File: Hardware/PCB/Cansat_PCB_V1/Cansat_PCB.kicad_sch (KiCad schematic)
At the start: 50 parts, among them J1 Lecteur SD, SW1 RSTBTN, SW2 boot, U1 Baro BMP581, U2 STM32G431CBUx, U3 IMU BNO055, U4 Adaptateur USB, Y1 Crystal_GND24_Small, Y2 Oscillateur_IMU

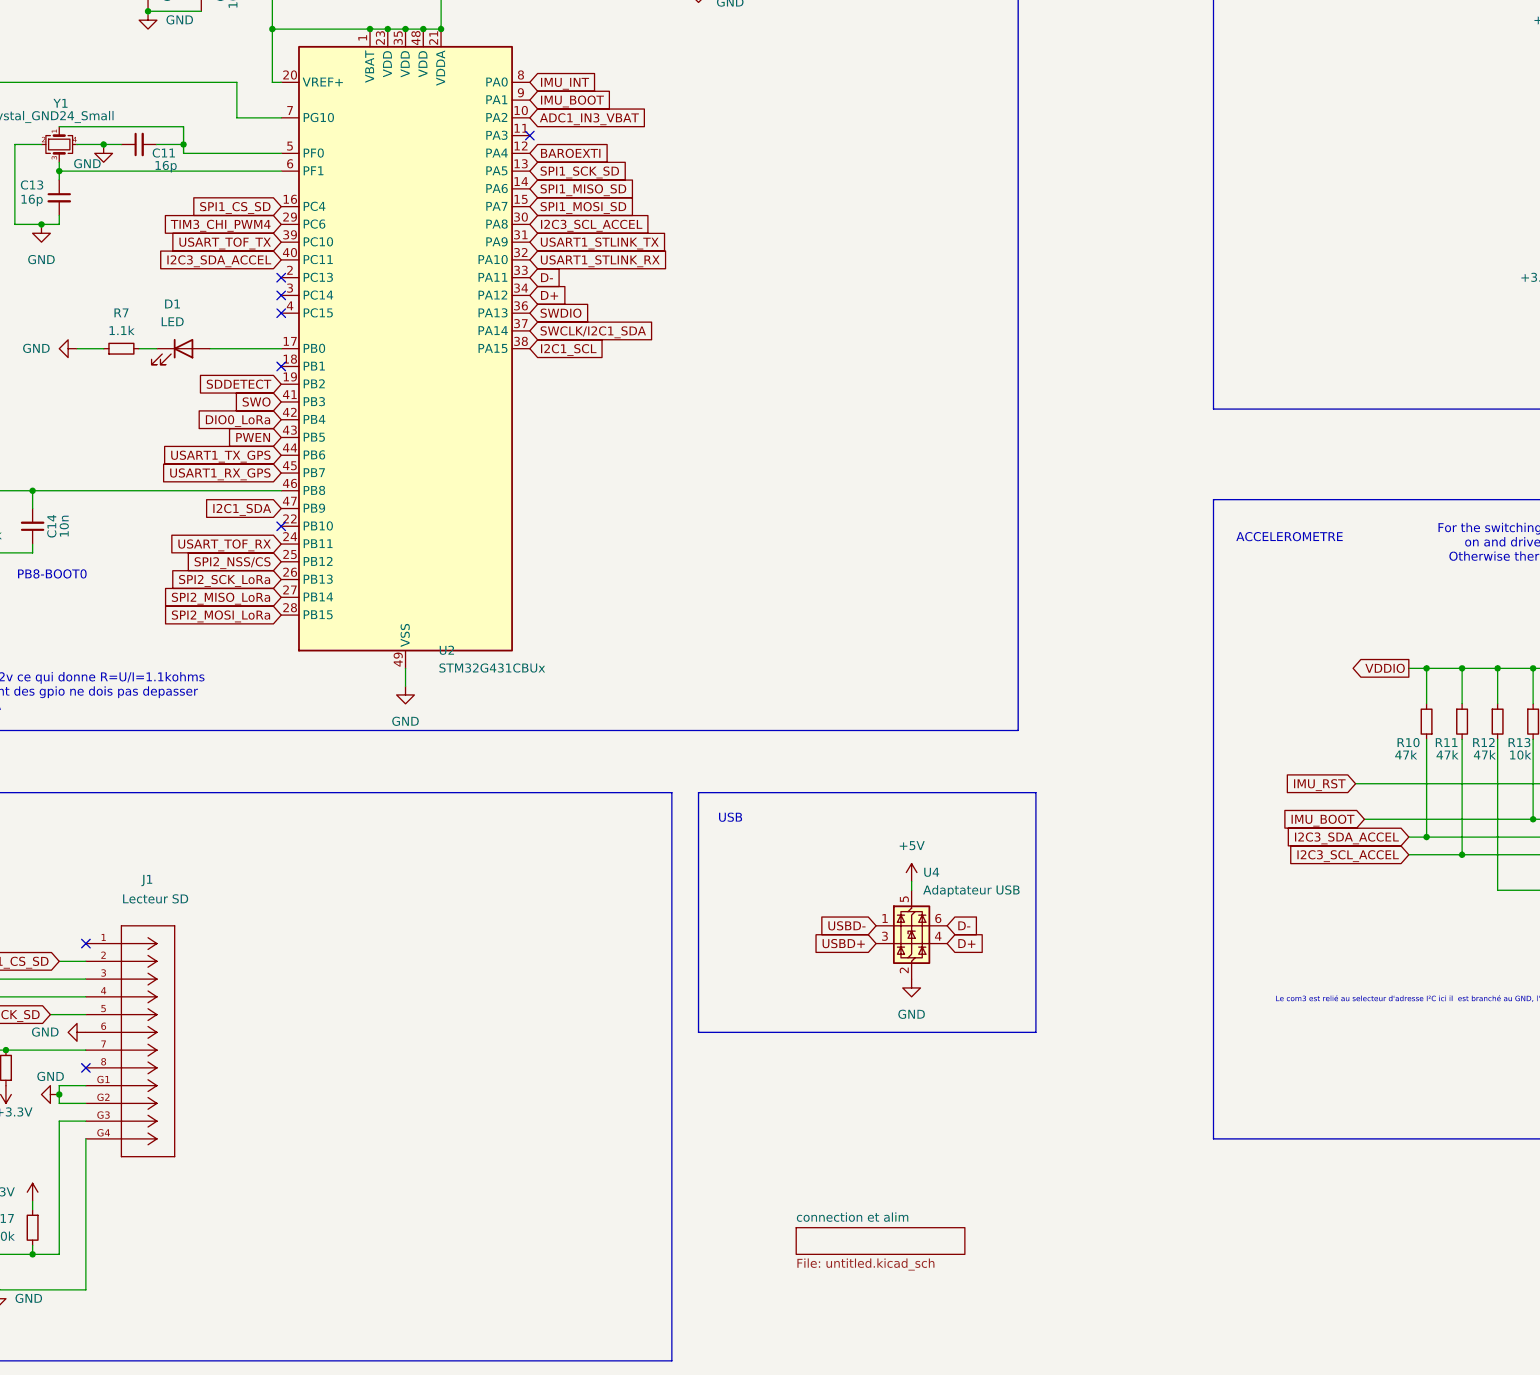
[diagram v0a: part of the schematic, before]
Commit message: ajout 2 Led adr + btn cmd + buck LMR51625 => sch complet sans warnings et erreurs
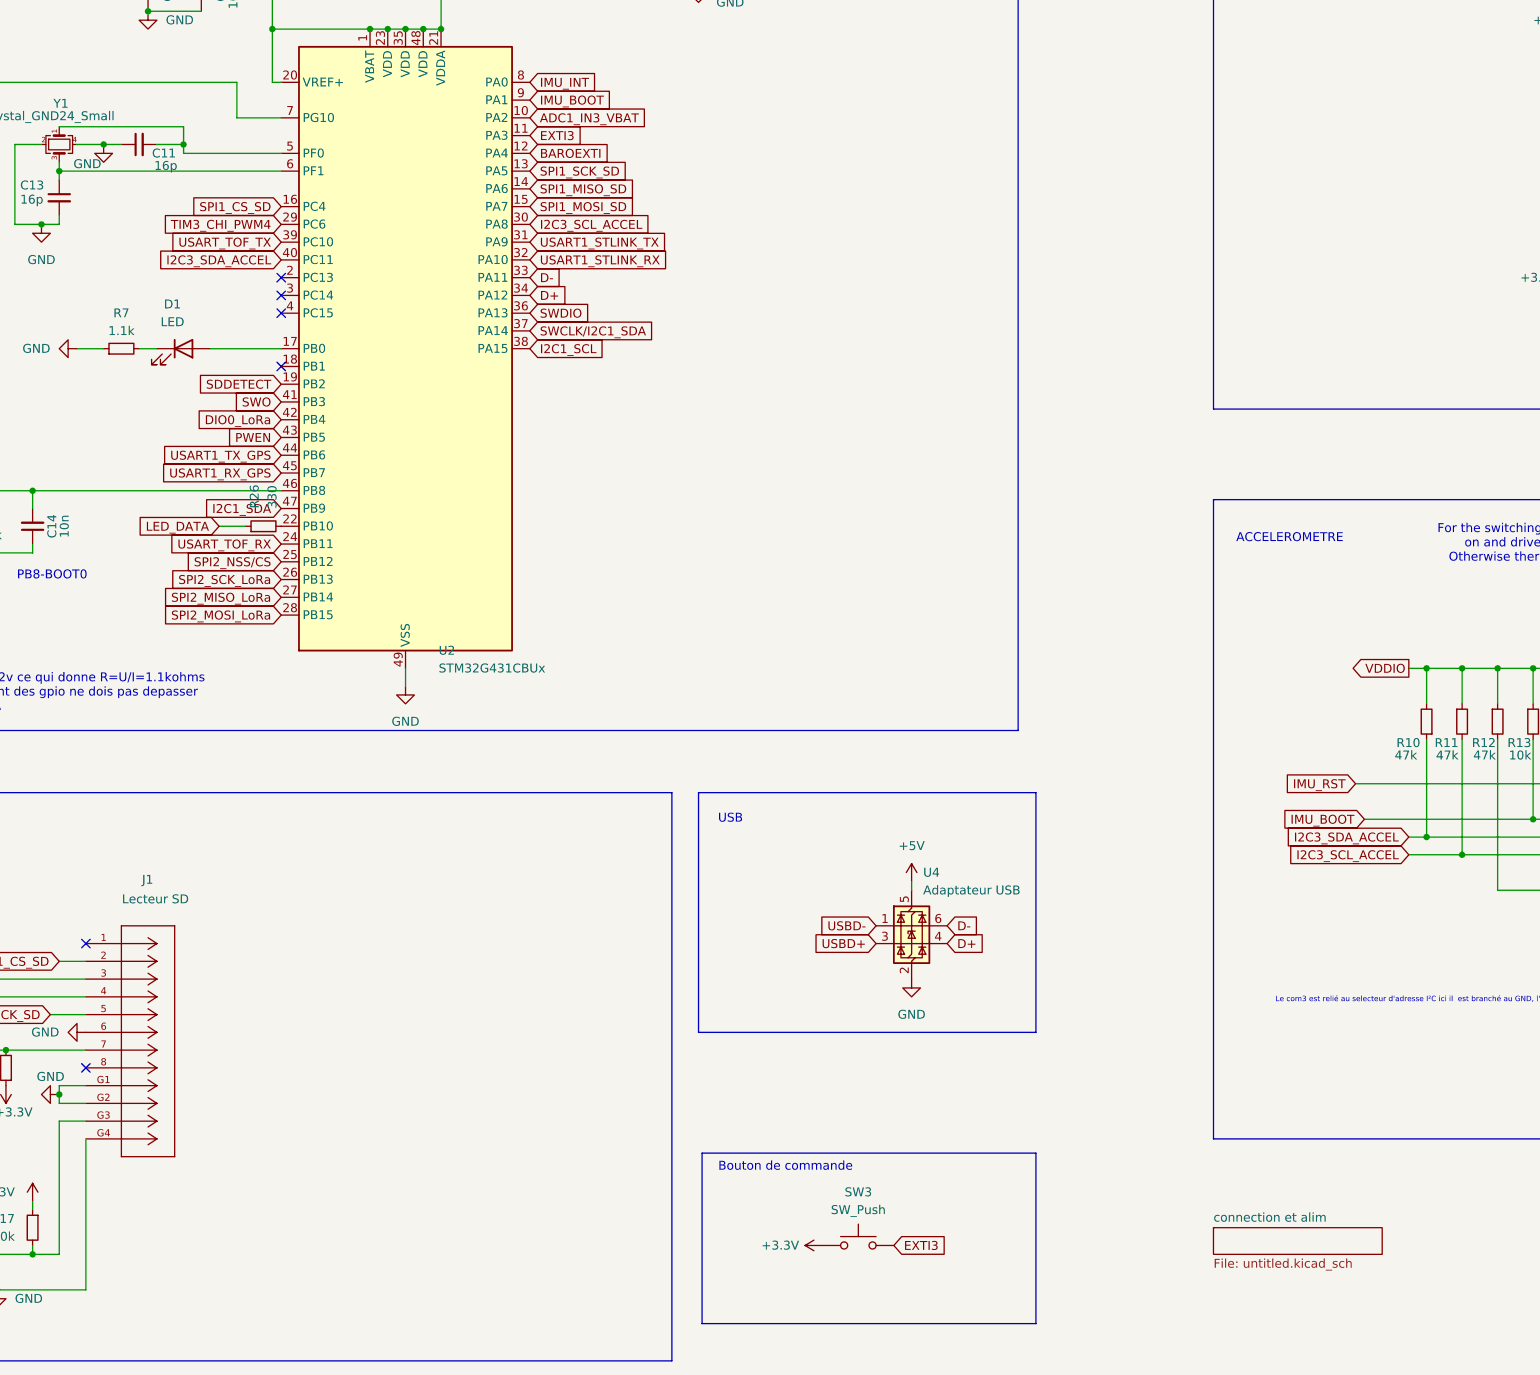
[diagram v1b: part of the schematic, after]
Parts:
- added R26: 330, Resistor_SMD:R_0402_1005Metric_Pad0.72x0.64mm_HandSolder, symbol Device:R_Small
- added SW3: SW_Push, Button_Switch_SMD:SW_Push_1P1T_NO_CK_PTS125Sx43PSMTR, symbol Switch:SW_Push
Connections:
- net +3.3V: now also SW3.1
- net EXTI3: now reaches U2.11 (PA3)
- net EXTI3: now also SW3.2
- net at U2.22 (PB10): now also R26.2
- new net LED_DATA: R26.1
- no-connect marks 12 -> 10
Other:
- note added: "Bouton de commande"

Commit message: routage non fini : ceci est un commit de transfert de fichier vers un autre PC
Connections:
- net VDDIO is gone; now on net +3.3V: C15.2, R10.2, R11.1, R12.1, R13.1, R14.1, U3.28 (VDDIO)
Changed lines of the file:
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@@
 	)
 	(junction
+		(at 340.36 149.86)
+		(diameter 0)
+		(color 0 0 0 0)
+	)
+	(junction
 		(at 320.04 87.63)
 		(diameter 0)
@@
 	)
 	(junction
-		(at 328.93 149.86)
-		(diameter 0)
-		(color 0 0 0 0)
-	)
-	(junction
 		(at 132.08 58.42)
 		(diameter 0)
@@
 	(wire
 		(pts
-			(xy 300.99 149.86) (xy 328.93 149.86)
-		)
-		(stroke
-			(width 0)
-			(type default)
-		)
-	)
-	(wire
-		(pts
 			(xy 77.47 204.47) (xy 88.9 204.47)
 		)
@@
 	(wire
 		(pts
+			(xy 340.36 149.86) (xy 356.87 149.86)
+		)
+		(stroke
+			(width 0)
+			(type default)
+		)
+	)
+	(wire
+		(pts
 			(xy 85.09 78.74) (xy 116.84 78.74)
 		)
@@
 	(wire
 		(pts
-			(xy 328.93 149.86) (xy 356.87 149.86)
+			(xy 300.99 149.86) (xy 340.36 149.86)
 		)
 		(stroke
@@
 	)
 	(symbol
+		(lib_id "power:+3.3V")
+		(at 340.36 149.86 0)
+		(unit 1)
+		(exclude_from_sim no)
+		(in_bom yes)
+		(on_board yes)
+		(dnp no)
+		(property "Reference" "#PWR041"
+			(at 340.36 153.67 0)
+			(effects
+				(font
+					(size 1.27 1.27)
+				)
+				(hide yes)
+			)
+		)
+		(property "Value" "+3.3V"
+			(at 336.55 146.05 0)
+			(effects
+				(font
+					(size 1.27 1.27)
+				)
+				(justify left)
+			)
+		)
+		(property "Footprint" ""
+			(at 340.36 149.86 0)
+			(effects
+				(font
+					(size 1.27 1.27)
+				)
+				(hide yes)
+			)
+		)
+		(property "Datasheet" ""
+			(at 340.36 149.86 0)
+			(effects
+				(font
+					(size 1.27 1.27)
+				)
+				(hide yes)
+			)
+		)
+		(property "Description" "Power symbol creates a global label with name \"+3.3V\""
+			(at 340.36 149.86 0)
+			(effects
+				(font
+					(size 1.27 1.27)
+				)
+				(hide yes)
+			)
+		)
+		(pin "1"
+		)
+		(instances
+			(project "Cansat_PCB"
+				(path "/43b9f51a-edfb-48c9-aab9-a28c7efe9297"
+					(reference "#PWR041")
+					(unit 1)
+				)
+			)
+		)
+	)
+	(symbol
 		(lib_id "Device:C_Small")
 		(at 96.52 74.93 90)
@@
 					(unit 1)
 				)
-			)
-		)
-	)
-	(symbol
-		(lib_id "power:PWR_FLAG")
-		(at 328.93 149.86 0)
-		(unit 1)
-		(exclude_from_sim no)
-		(in_bom yes)
-		(on_board yes)
-		(dnp no)
-		(fields_autoplaced yes)
-		(property "Reference" "#FLG03"
-			(at 328.93 147.955 0)
-			(effects
-				(font
-					(size 1.27 1.27)
-				)
-				(hide yes)
-			)
-		)
-		(property "Value" "PWR_FLAG"
-			(at 328.93 144.78 0)
-			(effects
-				(font
-					(size 1.27 1.27)
-				)
-			)
-		)
-		(property "Footprint" ""
-			(at 328.93 149.86 0)
-			(effects
-				(font
-					(size 1.27 1.27)
-				)
-				(hide yes)
-			)
-		)
-		(property "Datasheet" "~"
-			(at 328.93 149.86 0)
-			(effects
-				(font
-					(size 1.27 1.27)
-				)
-				(hide yes)
-			)
-		)
-		(property "Description" "Special symbol for telling ERC where power comes from"
-			(at 328.93 149.86 0)
-			(effects
-				(font
-					(size 1.27 1.27)
-				)
-				(hide yes)
-			)
-		)
-		(pin "1"
-		)
-		(instances
-			(project "Cansat_PCB"
-				(path "/43b9f51a-edfb-48c9-aab9-a28c7efe9297"
-					(reference "#FLG03")
-					(unit 1)
-				)

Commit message: nouvelles règles de routage Attention les pistes sont à l'ancienne taille : a corriger
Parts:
- removed SW3: SW_Push, Button_Switch_SMD:SW_Push_1P1T_NO_CK_PTS125Sx43PSMTR, symbol Switch:SW_Push
- removed U4: Adaptateur USB, footprints:SOT23-6L_STM, symbol Power_Protection:USBLC6-2SC6
- J1: symbol 473092651_&_BMP581_&_WSEN-ISDS_2536030320001:473092651 -> Homemade:473092651
- U1: footprint bmp581:BMP581 -> footprints:BMP581; symbol BMP581:BMP581 -> Homemade:BMP581
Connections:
- net D+: no longer names the net of U2.34 (PA12)
- net D-: no longer names the net of U2.33 (PA11)
- no-connect marks 10 -> 13
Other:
- note added: "VDDIO"
- note removed: "Bouton de commande"
- note removed: "USB"

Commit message: Début du routage
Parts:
- R10, R11, R12: value 47k -> 2.2k
- R13, R14: value 10k -> 2.2k
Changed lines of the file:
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@@
 			)
 		)
-		(property "Value" "47k"
+		(property "Value" "2.2k"
 			(at 276.098 162.306 0)
 			(effects
@@
 			)
 		)
-		(property "Value" "47k"
+		(property "Value" "2.2k"
 			(at 290.576 162.306 0)
 			(effects
@@
 			)
 		)
-		(property "Value" "47k"
+		(property "Value" "2.2k"
 			(at 285.242 162.306 0)
 			(effects
@@
 			)
 		)
-		(property "Value" "10k"
+		(property "Value" "2.2k"
 			(at 300.736 162.306 0)
 			(effects
@@
 			)
 		)
-		(property "Value" "10k"
+		(property "Value" "2.2k"
 			(at 295.656 162.306 0)
 			(effects
